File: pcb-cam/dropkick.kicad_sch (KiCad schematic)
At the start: 53 parts, among them J1 Conn_01x10, SW1 450405020524, SW2 KMR211NG_LFS, U1 SPX3819-3.3, U2 MCP73831T-2ACI/OT, U3 CAM-M8C-0, U4 ATSAMD21G18A-AUT, U5 DPS310XTSA1, U6 MPU-6050, X1 USB micro-B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

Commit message: V5-CAM PCB
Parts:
- removed H4: MountingHole, lib_fp:MOUNTINGHOLE_2.5_PLATED, symbol Mechanical:MountingHole
- removed R8, R9: 20, Resistor_SMD:R_0603_1608Metric, symbol Adafruit Feather M0 Adalogger-eagle-import:RESISTOR_0603_NOOUT
- CHG1, L1, L2: symbol Adafruit Feather M0 Adalogger-eagle-import:LED0805_NOOUTLINE -> Device:LED
- L3: renamed from D2; symbol Adafruit MPU6050-eagle-import:LED0603_NOOUTLINE -> Device:LED
- R6, R7: footprint Resistor_SMD:R_0603_1608Metric -> Resistor_SMD:R_0402_1005Metric
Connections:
- net D8: now also L1.2 (A); no longer L1.A
- net GND: now also L2.1 (K), L3.1 (K); no longer L2.C, L3.C, U6.THERM (THERMAL)
- net VBUS: now also CHG1.2 (A); no longer CHG1.A
- net at R10.2: now also L2.2 (A); no longer L2.A
- net at R5.1: now also CHG1.1 (K); no longer CHG1.C
- net at R12.2: now also L3.2 (A); no longer L3.A
- net at R11.1: now also L1.1 (K); no longer L1.C
- no-connect marks 26 -> 28

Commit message: V5-CAM add INT line to MPU6050
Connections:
- net INT is gone; now on net D11: U6.12 (INT)
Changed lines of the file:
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@@
+    (effects (font (size 1.27 1.27)) (justify left bottom))
+  )
+  (label "INT" (at 127 139.7 0)
     (effects (font (size 1.27 1.27)) (justify left bottom))
   )

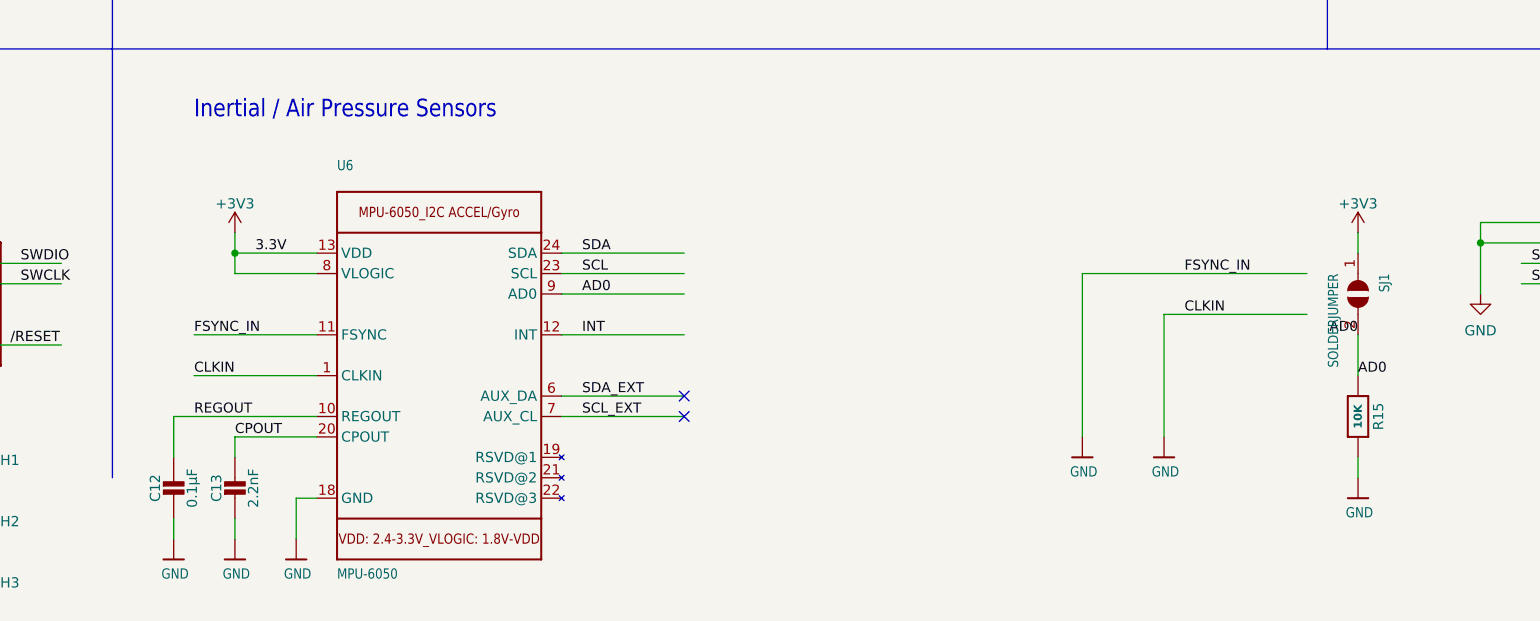
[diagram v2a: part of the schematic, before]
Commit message: Clean up AD0 address line for MPU6050
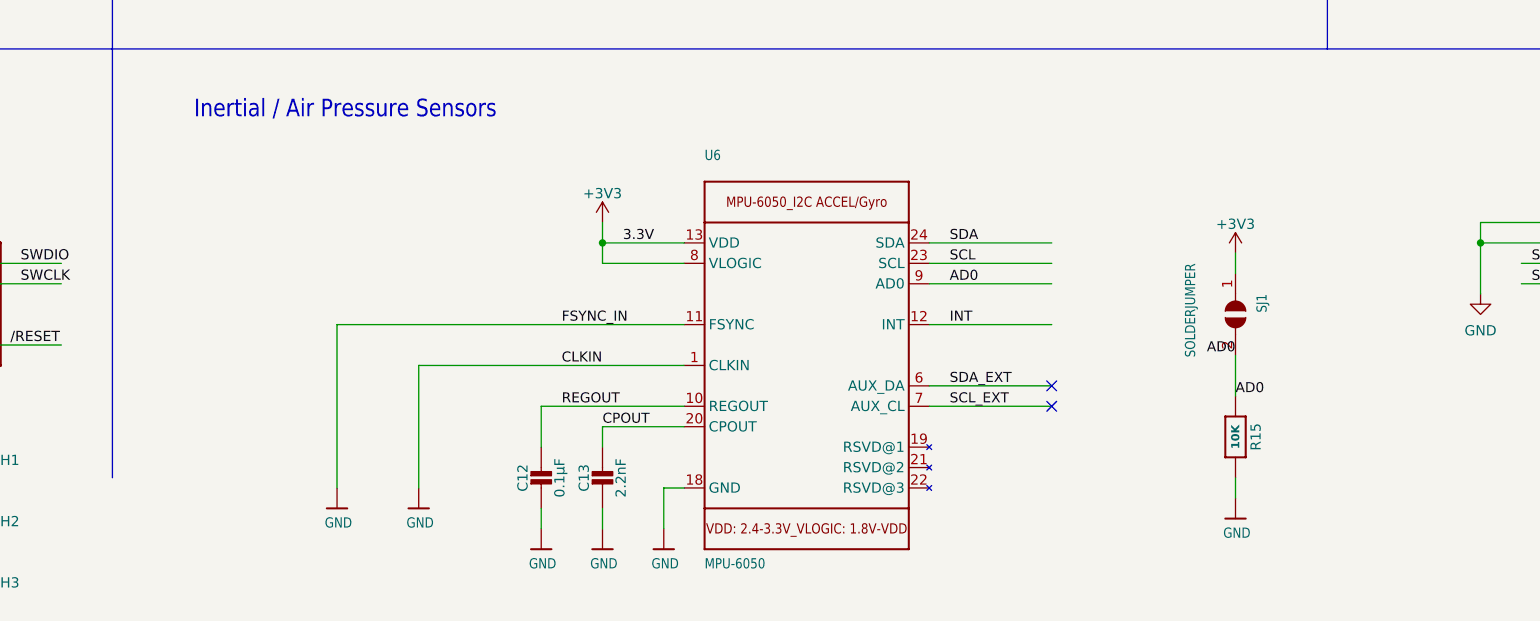
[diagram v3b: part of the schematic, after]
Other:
- moved on the sheet: C12, C13, R15, SJ1, U6

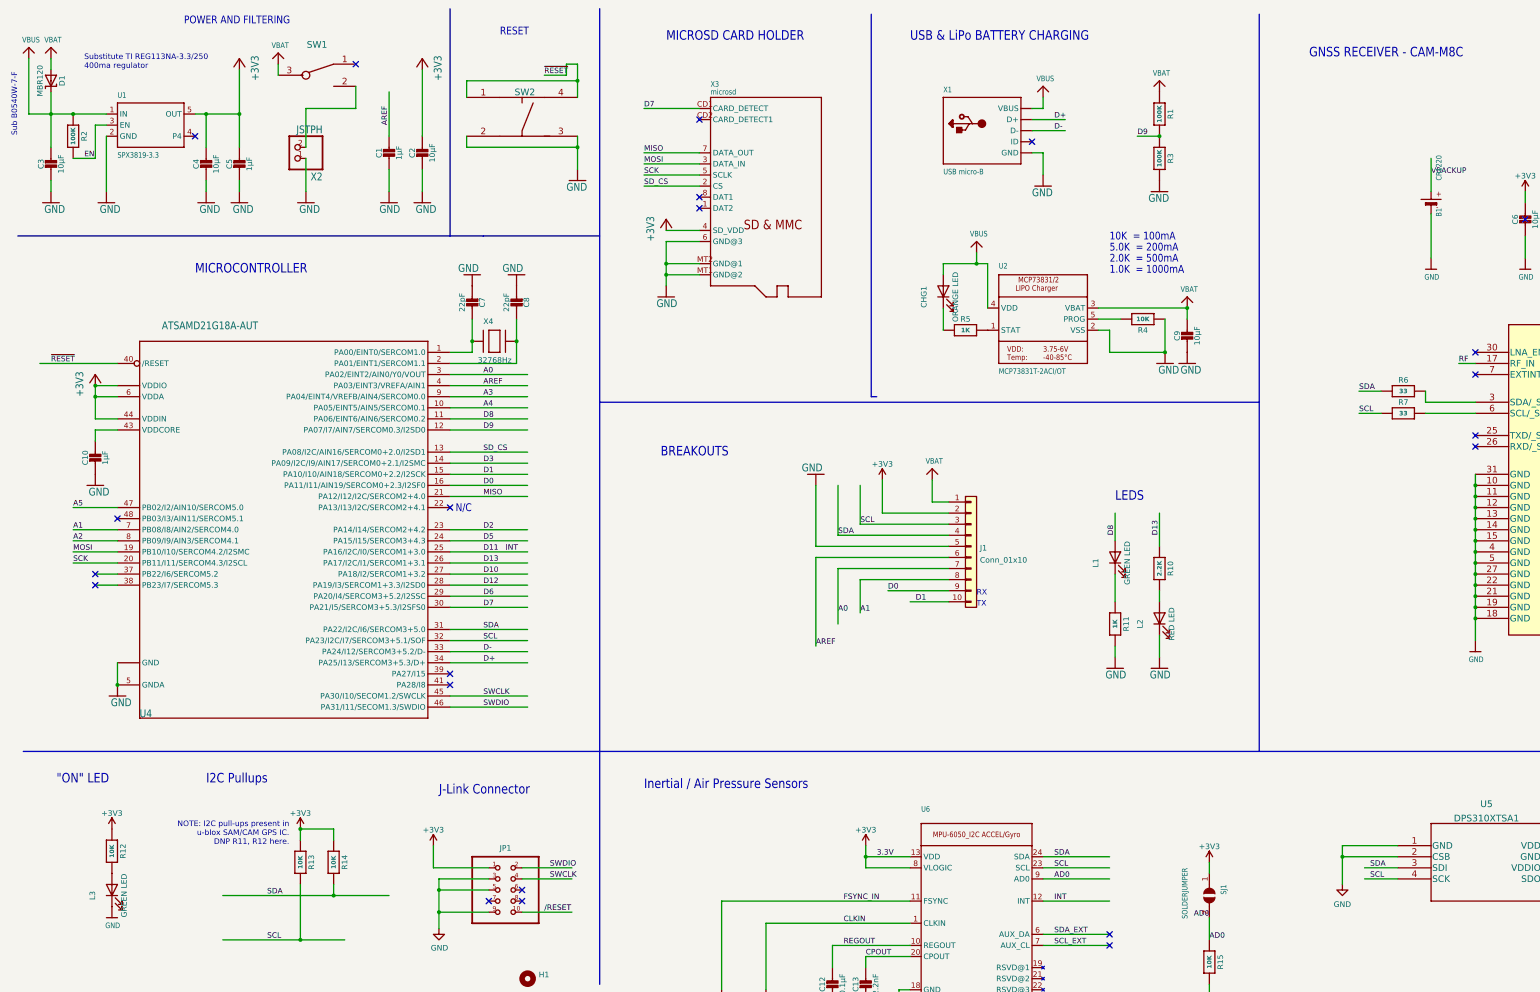
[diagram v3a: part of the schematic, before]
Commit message: Improve LED wiring consistency; update gerber
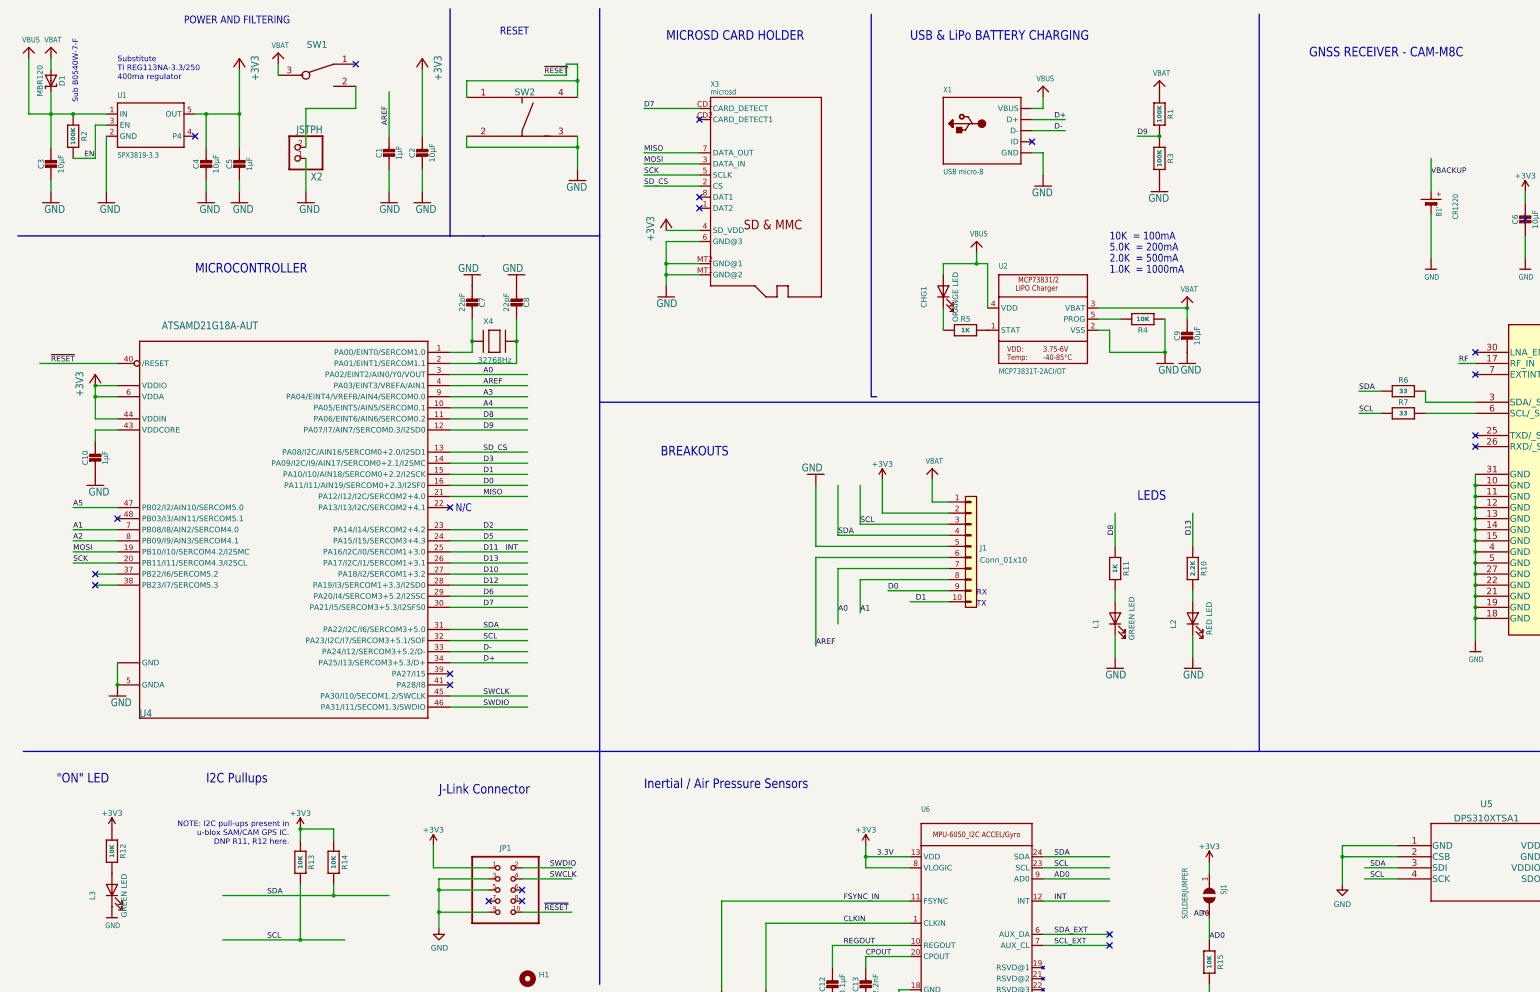
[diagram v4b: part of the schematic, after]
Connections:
- net /RESET is gone; now on net ~{RESET}: JP1.10
- net D8: now also R11.1; no longer L1.2 (A)
- net GND: now also L1.1 (K); no longer R11.2
- new net: L1.2 (A), R11.2
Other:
- moved on the sheet: L1, L2, R10, R11
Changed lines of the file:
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@@
+    (stroke (width 0) (type default) (color 0 0 0 0))
+  )
+  (wire (pts (xy 266.7 130.81) (xy 266.7 138.43))
     (stroke (width 0) (type default) (color 0 0 0 0))
   )
@@
     (stroke (width 0) (type default) (color 0 0 0 0))
   )
-  (wire (pts (xy 266.7 130.81) (xy 266.7 137.16))
-    (stroke (width 0) (type default) (color 0 0 0 0))
-  )
   (wire (pts (xy 318.77 207.01) (xy 318.77 209.55))
     (stroke (width 0) (type default) (color 0 0 0 0))
@@
     (stroke (width 0) (type default) (color 0 0 0 0))
   )
-  (wire (pts (xy 266.7 161.29) (xy 266.7 163.83))
-    (stroke (width 0) (type default) (color 0 0 0 0))
-  )
   (wire (pts (xy 114.3 99.06) (xy 132.08 99.06))
     (stroke (width 0) (type default) (color 0 0 0 0))
@@
     (stroke (width 0) (type default) (color 0 0 0 0))
   )
-  (wire (pts (xy 266.7 144.78) (xy 266.7 151.13))
-    (stroke (width 0) (type default) (color 0 0 0 0))
-  )
   (wire (pts (xy 250.19 38.1) (xy 250.19 35.56))
     (stroke (width 0) (type default) (color 0 0 0 0))
@@
     (stroke (width 0) (type default) (color 0 0 0 0))
   )
-  (wire (pts (xy 276.86 158.75) (xy 276.86 163.83))
+  (wire (pts (xy 284.48 158.75) (xy 284.48 163.83))
     (stroke (width 0) (type default) (color 0 0 0 0))
   )
@@
     (stroke (width 0) (type default) (color 0 0 0 0))
   )
-  (wire (pts (xy 276.86 138.43) (xy 276.86 130.81))
+  (wire (pts (xy 284.48 138.43) (xy 284.48 130.81))
     (stroke (width 0) (type default) (color 0 0 0 0))
   )
@@
     (stroke (width 0) (type default) (color 0 0 0 0))
   )
+  (wire (pts (xy 266.7 148.59) (xy 266.7 151.13))
+    (stroke (width 0) (type default) (color 0 0 0 0))
+  )
   (polyline (pts (xy 148.59 105.41) (xy 299.72 105.41))
     (stroke (width 0) (type default) (color 0 0 0 0))
@@
     (stroke (width 0) (type default) (color 0 0 0 0))
   )
+  (wire (pts (xy 266.7 158.75) (xy 266.7 163.83))
+    (stroke (width 0) (type default) (color 0 0 0 0))
+  )
   (wire (pts (xy 17.78 39.37) (xy 22.86 39.37))
     (stroke (width 0) (type default) (color 0 0 0 0))
@@
     (stroke (width 0) (type default) (color 0 0 0 0))
   )
-  (wire (pts (xy 276.86 148.59) (xy 276.86 151.13))
+  (wire (pts (xy 284.48 148.59) (xy 284.48 151.13))
     (stroke (width 0) (type default) (color 0 0 0 0))
   )
@@
     (effects (font (size 2.1844 1.8567)) (justify left bottom))
   )
-  (text "Substitute TI REG113NA-3.3/250\n400ma regulator\n" (at 30.48 29.21 0)
+  (text "Substitute \nTI REG113NA-3.3/250\n400ma regulator\n" (at 38.1 31.75 0)
     (effects (font (size 1.27 1.27)) (justify left bottom))
   )
-  (text "LEDS" (at 266.7 128.27 180)
+  (text "LEDS" (at 271.78 128.27 180)
     (effects (font (size 2.1844 1.8567)) (justify left bottom))
   )
@@
     (effects (font (size 1.27 1.27)) (justify right bottom))
   )
-  (text "Sub B0540W-7-F" (at 15.24 44.45 90)
+  (text "Sub B0540W-7-F" (at 29.21 36.83 90)
     (effects (font (size 1.27 1.27)) (justify left bottom))
   )
@@
     (effects (font (size 1.2446 1.2446)) (justify left bottom))
   )
-  (label "D13" (at 276.86 135.89 90)
+  (label "D13" (at 284.48 135.89 90)
     (effects (font (size 1.2446 1.2446)) (justify left bottom))
   )
@@
     (effects (font (size 1.2446 1.2446)) (justify left bottom))
   )
-  (label "{slash}RESET" (at 135.89 222.25 0)
+  (label "~{RESET}" (at 135.89 222.25 0)
     (effects (font (size 1.27 1.27)) (justify left bottom))
   )
@@
     (pin "1")
   )
-  (symbol (lib_id "Adafruit Feather M0 Adalogger-eagle-import:RESISTOR_0603_NOOUT") (at 276.86 143.51 270) (unit 1)
-    (in_bom yes) (on_board yes)
-    (property "Reference" "R10" (id 0) (at 279.4 143.51 0))
-    (property "Value" "2.2K" (id 1) (at 276.86 143.51 0)
+  (symbol (lib_id "Adafruit Feather M0 Adalogger-eagle-import:RESISTOR_0603_NOOUT") (at 284.48 143.51 270) (unit 1)
+    (in_bom yes) (on_board yes)
+    (property "Reference" "R10" (id 0) (at 287.02 143.51 0))
+    (property "Value" "2.2K" (id 1) (at 284.48 143.51 0)
       (effects (font (size 1.016 1.016) bold))
     )
-    (property "Footprint" "Resistor_SMD:R_0603_1608Metric" (id 2) (at 276.86 143.51 0)
-      (effects (font (size 1.27 1.27)) hide)
-    )
-    (property "Datasheet" "" (id 3) (at 276.86 143.51 0)
-      (effects (font (size 1.27 1.27)) hide)
-    )
-    (property "Manufacturer Part" "CRCW06032K20FKEAHP" (id 4) (at 276.86 143.51 0)
+    (property "Footprint" "Resistor_SMD:R_0603_1608Metric" (id 2) (at 284.48 143.51 0)
+      (effects (font (size 1.27 1.27)) hide)
+    )
+    (property "Datasheet" "" (id 3) (at 284.48 143.51 0)
+      (effects (font (size 1.27 1.27)) hide)
+    )
+    (property "Manufacturer Part" "CRCW06032K20FKEAHP" (id 4) (at 284.48 143.51 0)
       (effects (font (size 1.27 1.27)) hide)
     )
@@
       (effects (font (size 1.27 1.0795)) (justify left bottom))
     )
-    (property "Value" "CR1220" (id 1) (at 341.63 54.61 0)
+    (property "Value" "CR1220" (id 1) (at 345.44 63.5 0)
       (effects (font (size 1.27 1.0795)) (justify left bottom))
     )
@@
     (pin "-")
   )
-  (symbol (lib_id "Adafruit Feather M0 Adalogger-eagle-import:RESISTOR_0603_NOOUT") (at 266.7 156.21 270) (unit 1)
-    (in_bom yes) (on_board yes)
-    (property "Reference" "R11" (id 0) (at 269.24 156.21 0))
-    (property "Value" "1K" (id 1) (at 266.7 156.21 0)
+  (symbol (lib_id "Adafruit Feather M0 Adalogger-eagle-import:RESISTOR_0603_NOOUT") (at 266.7 143.51 270) (unit 1)
+    (in_bom yes) (on_board yes)
+    (property "Reference" "R11" (id 0) (at 269.24 143.51 0))
+    (property "Value" "1K" (id 1) (at 266.7 143.51 0)
       (effects (font (size 1.016 1.016) bold))
     )
-    (property "Footprint" "Resistor_SMD:R_0603_1608Metric" (id 2) (at 266.7 156.21 0)
-      (effects (font (size 1.27 1.27)) hide)
-    )
-    (property "Datasheet" "" (id 3) (at 266.7 156.21 0)
+    (property "Footprint" "Resistor_SMD:R_0603_1608Metric" (id 2) (at 266.7 143.51 0)
+      (effects (font (size 1.27 1.27)) hide)
+    )
+    (property "Datasheet" "" (id 3) (at 266.7 143.51 0)
       (effects (font (size 1.27 1.27)) hide)
     )
@@
     (pin "1")
   )
-  (symbol (lib_id "Device:LED") (at 266.7 140.97 90) (unit 1)
-    (in_bom yes) (on_board yes)
-    (property "Reference" "L1" (id 0) (at 262.255 142.24 0))
-    (property "Value" "GREEN LED" (id 1) (at 269.494 142.24 0))
-    (property "Footprint" "LED_SMD:LED_0603_1608Metric" (id 2) (at 266.7 140.97 0)
-      (effects (font (size 1.27 1.27)) hide)
-    )
-    (property "Datasheet" "" (id 3) (at 266.7 140.97 0)
-      (effects (font (size 1.27 1.27)) hide)
-    )
-    (property "Manufacturer Part" "LTST-S270KGKT" (id 4) (at 266.7 140.97 0)
+  (symbol (lib_id "Device:LED") (at 266.7 154.94 90) (unit 1)
+    (in_bom yes) (on_board yes)
+    (property "Reference" "L1" (id 0) (at 262.255 156.21 0))
+    (property "Value" "GREEN LED" (id 1) (at 270.51 154.94 0))
+    (property "Footprint" "LED_SMD:LED_0603_1608Metric" (id 2) (at 266.7 154.94 0)
+      (effects (font (size 1.27 1.27)) hide)
+    )
+    (property "Datasheet" "" (id 3) (at 266.7 154.94 0)
+      (effects (font (size 1.27 1.27)) hide)
+    )
+    (property "Manufacturer Part" "LTST-S270KGKT" (id 4) (at 266.7 154.94 0)
       (effects (font (size 1.27 1.27)) hide)
     )
@@
     (pin "2")
   )
-  (symbol (lib_id "Device:LED") (at 276.86 154.94 90) (unit 1)
-    (in_bom yes) (on_board yes)
-    (property "Reference" "L2" (id 0) (at 272.415 156.21 0))
-    (property "Value" "RED LED" (id 1) (at 279.654 156.21 0))
-    (property "Footprint" "LED_SMD:LED_0603_1608Metric" (id 2) (at 276.86 154.94 0)
-      (effects (font (size 1.27 1.27)) hide)
-    )
-    (property "Datasheet" "" (id 3) (at 276.86 154.94 0)
-      (effects (font (size 1.27 1.27)) hide)
-    )
-    (property "Manufacturer Part" "LTST-S270KRKT" (id 4) (at 276.86 154.94 0)
+  (symbol (lib_id "Device:LED") (at 284.48 154.94 90) (unit 1)
+    (in_bom yes) (on_board yes)
+    (property "Reference" "L2" (id 0) (at 280.035 156.21 0))
+    (property "Value" "RED LED" (id 1) (at 288.29 154.94 0))
+    (property "Footprint" "LED_SMD:LED_0603_1608Metric" (id 2) (at 284.48 154.94 0)
+      (effects (font (size 1.27 1.27)) hide)
+    )
+    (property "Datasheet" "" (id 3) (at 284.48 154.94 0)
+      (effects (font (size 1.27 1.27)) hide)
+    )
+    (property "Manufacturer Part" "LTST-S270KRKT" (id 4) (at 284.48 154.94 0)
       (effects (font (size 1.27 1.27)) hide)
     )
@@
     (pin "1")
   )
-  (symbol (lib_id "Adafruit Feather M0 Adalogger-eagle-import:GND") (at 276.86 166.37 0) (mirror y) (unit 1)
-    (in_bom yes) (on_board yes)
-    (property "Reference" "#GND07" (id 0) (at 276.86 166.37 0)
-      (effects (font (size 1.27 1.27)) hide)
-    )
-    (property "Value" "GND" (id 1) (at 279.4 168.91 0)
-      (effects (font (size 1.778 1.5113)) (justify left bottom))
-    )
-    (property "Footprint" "" (id 2) (at 276.86 166.37 0)
-      (effects (font (size 1.27 1.27)) hide)
-    )
-    (property "Datasheet" "" (id 3) (at 276.86 166.37 0)
-      (effects (font (size 1.27 1.27)) hide)
-    )
+  (symbol (lib_id "Adafruit Feather M0 Adalogger-eagle-import:GND") (at 284.48 166.37 0) (mirror y) (unit 1)
+    (in_bom yes) (on_board yes)
+    (property "Reference" "#GND07" (id 0) (at 284.48 166.37 0)
+      (effects (font (size 1.27 1.27)) hide)
+    )
+    (property "Value" "GND" (id 1) (at 287.02 168.91 0)
+      (effects (font (size 1.778 1.5113)) (justify left bottom))
+    )
+    (property "Footprint" "" (id 2) (at 284.48 166.37 0)
+      (effects (font (size 1.27 1.27)) hide)
+    )
+    (property "Datasheet" "" (id 3) (at 284.48 166.37 0)
+      (effects (font (size 1.27 1.27)) hide)
+    )
